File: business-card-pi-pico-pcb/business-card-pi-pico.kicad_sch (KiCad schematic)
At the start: 44 parts, among them U1 Pico

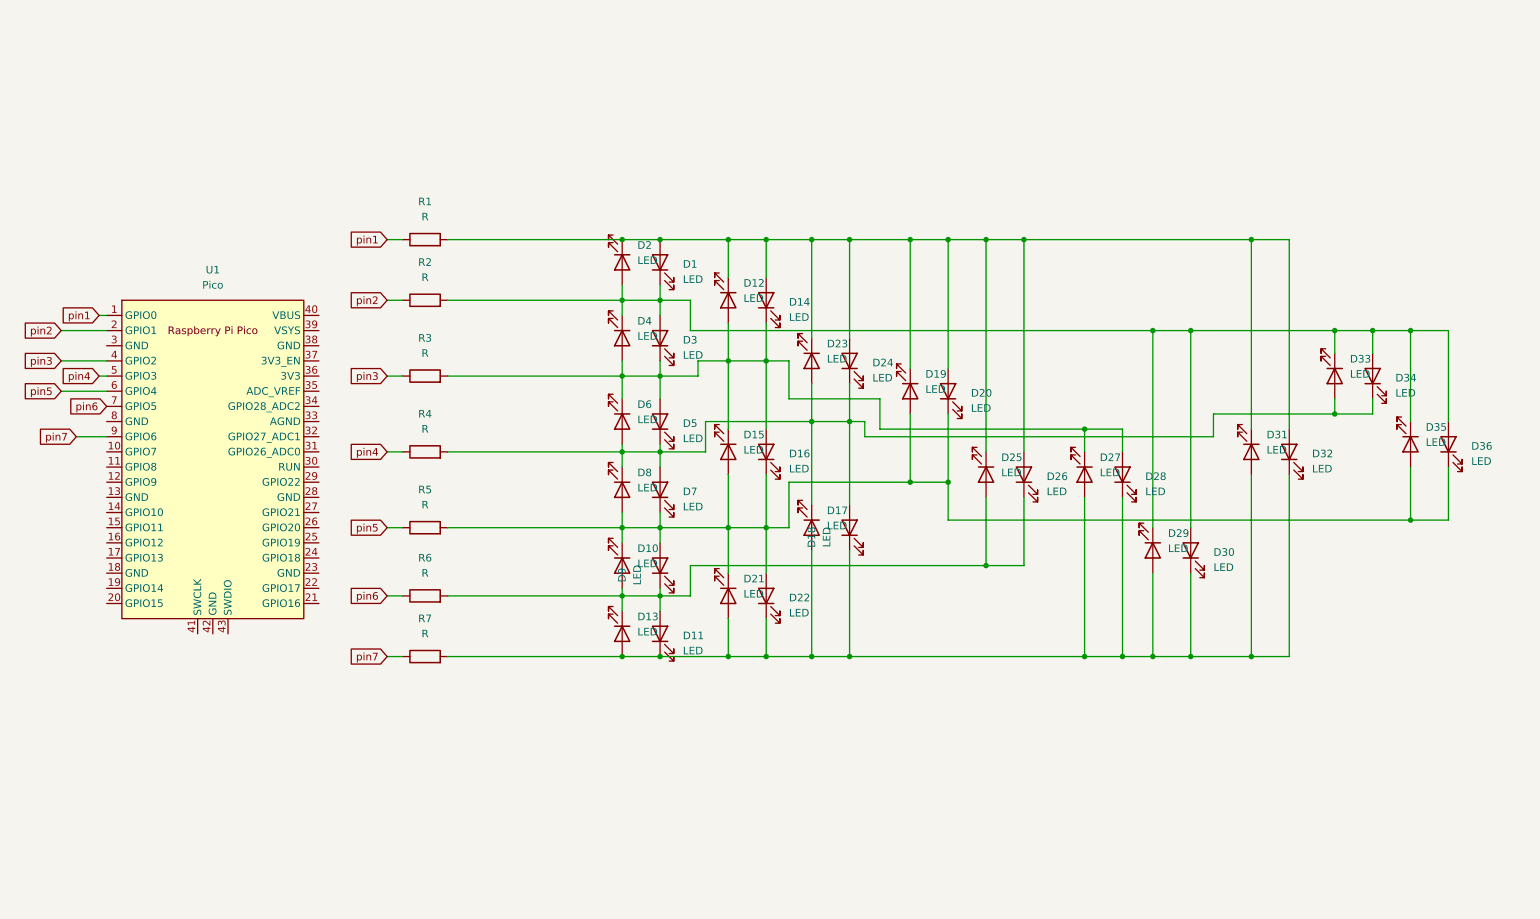
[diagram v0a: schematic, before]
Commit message: added SSD13006 display
added SSD13006 display and push button
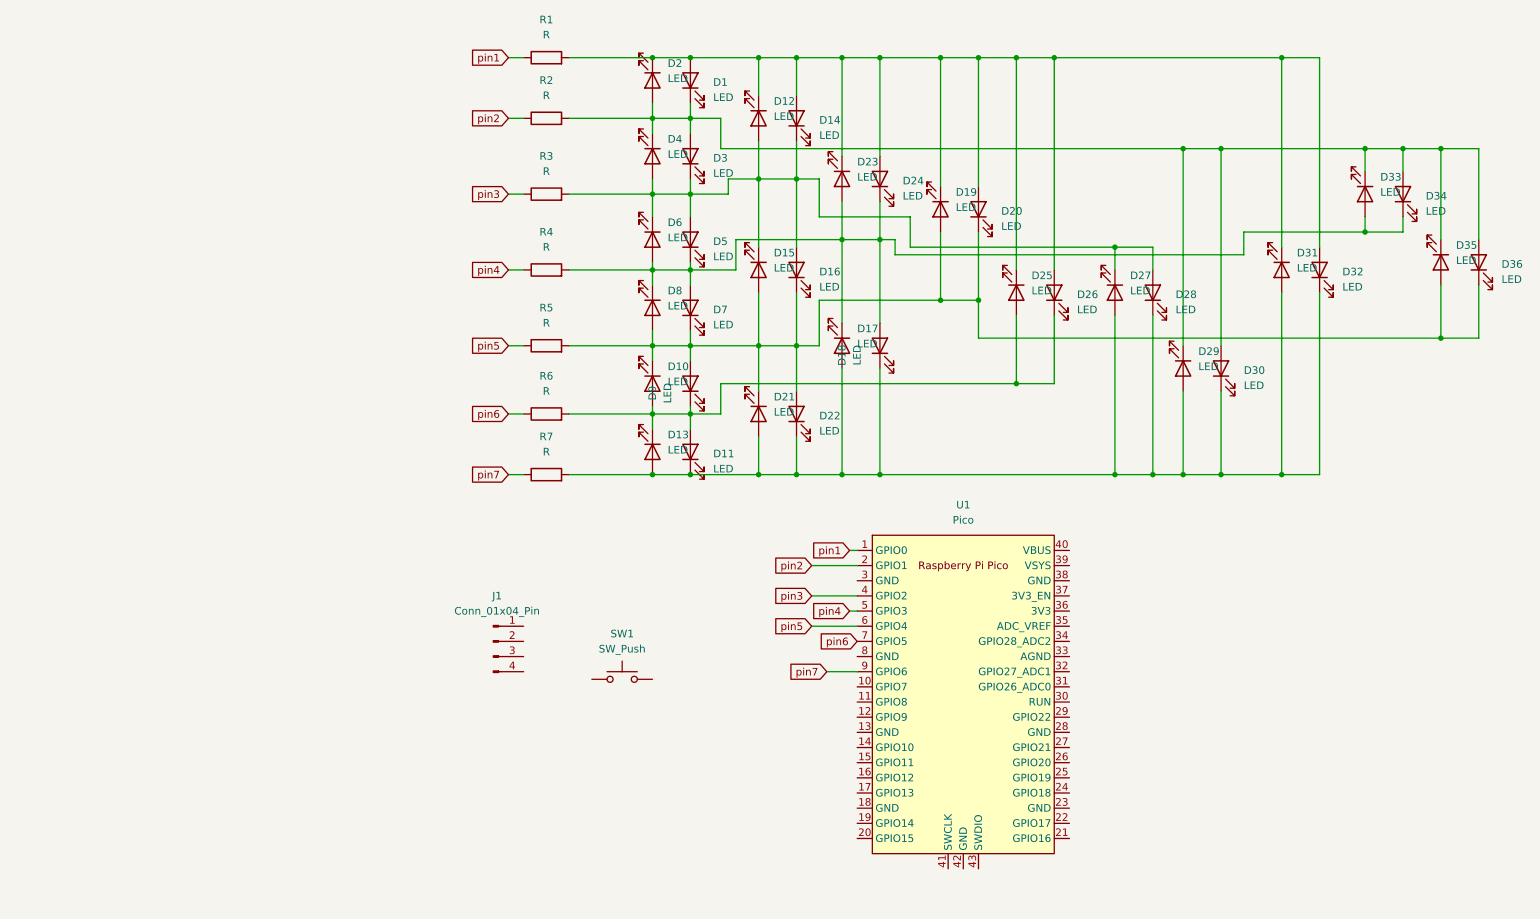
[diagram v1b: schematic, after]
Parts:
- added J1: Conn_01x04_Pin, Display:Adafruit_SSD1306, symbol Connector:Conn_01x04_Pin
- added SW1: SW_Push, Button_Switch_THT:SW_PUSH_6mm_H8mm, symbol Switch:SW_Push
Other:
- moved on the sheet: D1, D10, D11, D12, D13, D14, D15, D16, D17, D18, D19, D2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

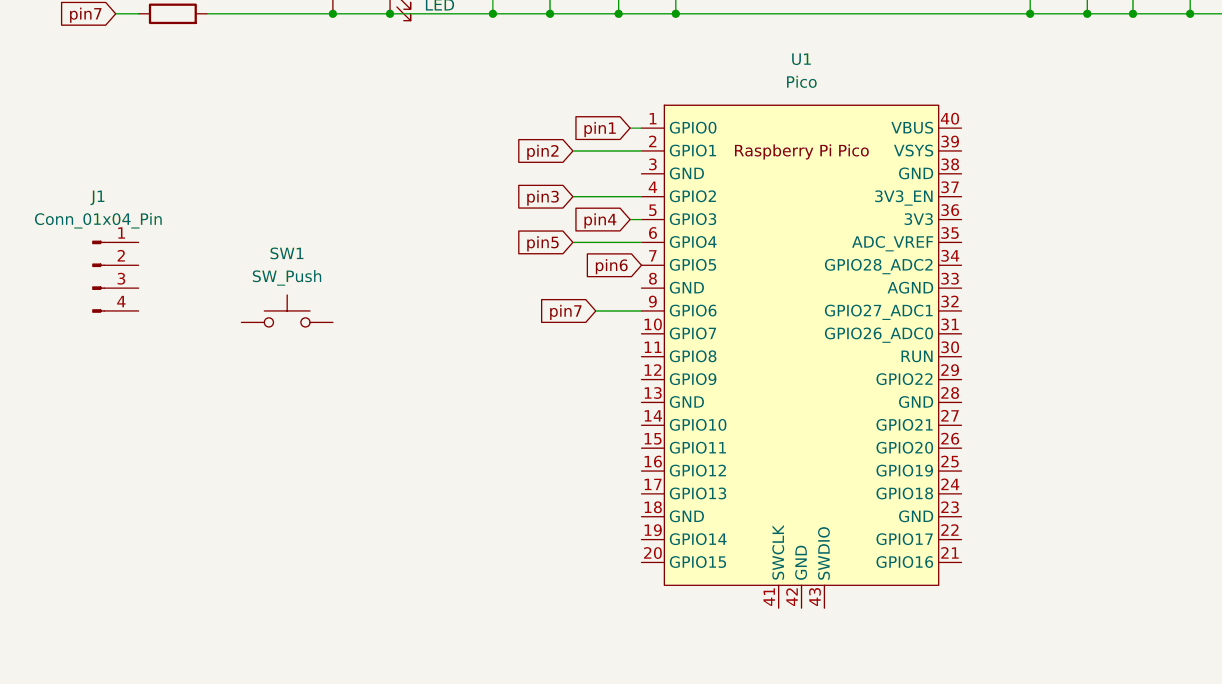
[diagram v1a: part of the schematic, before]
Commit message: Continue working on PCB
Continue working on PCB, added button/touch input pin
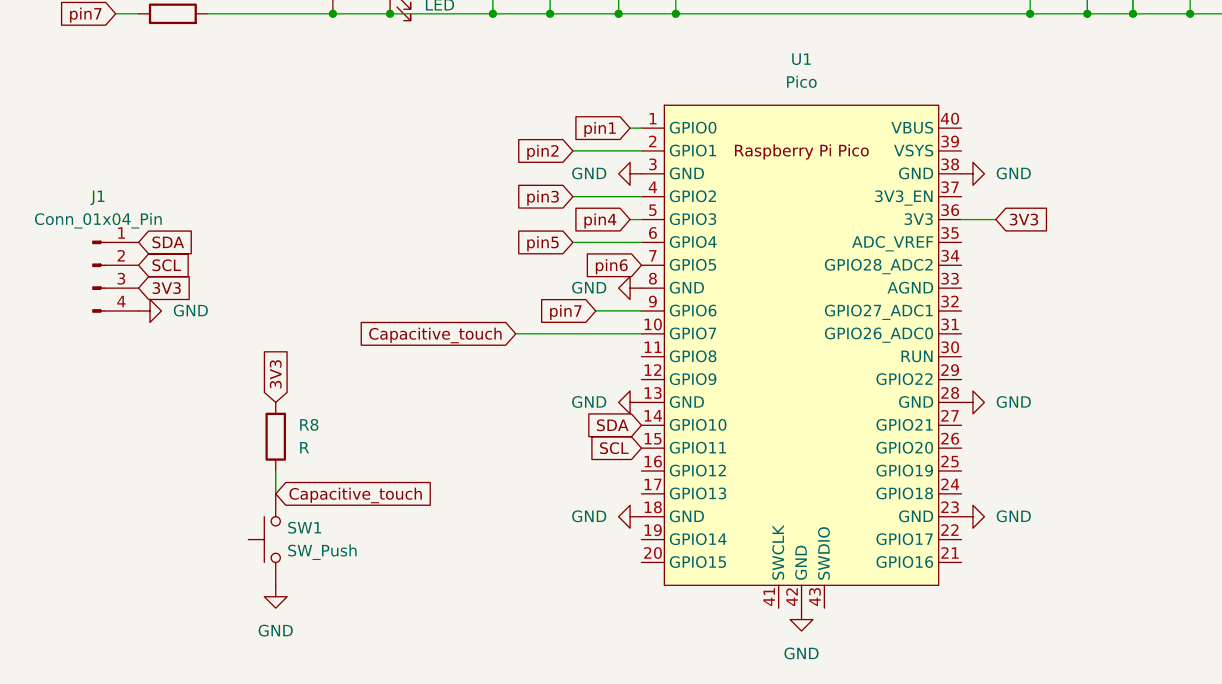
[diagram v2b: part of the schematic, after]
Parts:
- added R8: R, Resistor_SMD:R_0805_2012Metric, symbol Device:R
- J1: footprint Display:Adafruit_SSD1306 -> SSD1306:128x64OLED
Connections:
- net Capacitive_touch: now reaches U1.10 (GPIO7)
- net Capacitive_touch: now also SW1.2, R8.1
- net GND: now reaches U1.13 (GND)
- net GND: now also J1.4 (Pin_4), SW1.1, U1.18 (GND), U1.23 (GND), U1.28 (GND), U1.3 (GND), U1.38 (GND), U1.42 (GND), U1.8 (GND)
- net SDA: now reaches U1.14 (GPIO10)
- net SDA: now also J1.1 (Pin_1)
- net SCL: now reaches U1.15 (GPIO11)
- net SCL: now also J1.2 (Pin_2)
- net 3V3: now reaches U1.36 (3V3)
- net 3V3: now also J1.3 (Pin_3), R8.2
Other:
- moved on the sheet: SW1

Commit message: updated PCB
updated PCB
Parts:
- added R9: R, Resistor_SMD:R_0805_2012Metric, symbol Device:R
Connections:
- net Capacitive_touch: now also R9.2; no longer R8.1, SW1.2
- new net: R8.1, R9.1, SW1.2
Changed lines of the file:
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@@
 	)
 	(junction
+		(at 129.54 142.24)
+		(diameter 0)
+		(color 0 0 0 0)
+	)
+	(junction
 		(at 173.99 91.44)
 		(diameter 0)
@@
 	(wire
 		(pts
+			(xy 129.54 142.24) (xy 129.54 144.78)
+		)
+		(stroke
+			(width 0)
+			(type default)
+		)
+	)
+	(wire
+		(pts
 			(xy 173.99 52.07) (xy 173.99 66.04)
 		)
@@
 	(wire
 		(pts
-			(xy 129.54 142.24) (xy 129.54 144.78)
-		)
-		(stroke
-			(width 0)
-			(type default)
-		)
-	)
-	(wire
-		(pts
 			(xy 160.02 69.85) (xy 160.02 77.47)
 		)
@@
 	(wire
 		(pts
+			(xy 129.54 142.24) (xy 133.35 142.24)
+		)
+		(stroke
+			(width 0)
+			(type default)
+		)
+	)
+	(wire
+		(pts
 			(xy 121.92 31.75) (xy 135.89 31.75)
 		)
@@
 		)
 	)
+	(global_label "Capacitive_touch"
+		(shape input)
+		(at 140.97 142.24 0)
+		(fields_autoplaced yes)
+		(effects
+			(font
+				(size 1.27 1.27)
+			)
+			(justify left)
+		)
+		(property "Intersheetrefs" "${INTERSHEET_REFS}"
+			(at 159.9812 142.24 0)
+			(effects
+				(font
+					(size 1.27 1.27)
+				)
+				(justify left)
+				(hide yes)
+			)
+		)
+	)
 	(global_label "pin5"
 		(shape input)
@@
 		)
 	)
-	(global_label "Capacitive_touch"
-		(shape input)
-		(at 129.54 144.78 0)
-		(fields_autoplaced yes)
-		(effects
-			(font
-				(size 1.27 1.27)
-			)
-			(justify left)
-		)
-		(property "Intersheetrefs" "${INTERSHEET_REFS}"
-			(at 148.5512 144.78 0)
-			(effects
-				(font
-					(size 1.27 1.27)
-				)
-				(justify left)
-				(hide yes)
-			)
-		)
-	)
 	(global_label "pin7"
 		(shape input)
@@
 					(unit 1)
 				)
+			)
+		)
+	)
+	(symbol
+		(lib_id "Device:R")
+		(at 137.16 142.24 90)
+		(unit 1)
+		(exclude_from_sim no)
+		(in_bom yes)
+		(on_board yes)
+		(dnp no)
+		(fields_autoplaced yes)
+		(property "Reference" "R9"
+			(at 137.16 135.89 90)
+			(effects
+				(font
+					(size 1.27 1.27)
+				)
+			)
+		)
+		(property "Value" "R"
+			(at 137.16 138.43 90)
+			(effects
+				(font
+					(size 1.27 1.27)
+				)
+			)
+		)
+		(property "Footprint" "Resistor_SMD:R_0805_2012Metric"
+			(at 137.16 144.018 90)
+			(effects
+				(font
+					(size 1.27 1.27)
+				)
+				(hide yes)
+			)
+		)
+		(property "Datasheet" "~"
+			(at 137.16 142.24 0)
+			(effects
+				(font
+					(size 1.27 1.27)
+				)
+				(hide yes)
+			)
+		)
+		(property "Description" "Resistor"
+			(at 137.16 142.24 0)
+			(effects
+				(font
+					(size 1.27 1.27)
+				)
+				(hide yes)
+			)
+		)
+		(pin "2"
+		)
+		(pin "1"
+		)
+		(instances
+			(project "business-card-pi-pico"
+				(path "/3e5122c1-1f9e-4892-9d66-f0f99c7e104b"
+					(reference "R9")
+					(unit 1)
+				)

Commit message: backups
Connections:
- net 3V3: now also J1.1 (Pin_1); no longer J1.3 (Pin_3)
- net GND: now also J1.2 (Pin_2); no longer J1.4 (Pin_4)
- net SCL: now also J1.3 (Pin_3); no longer J1.2 (Pin_2)
- net SDA: now also J1.4 (Pin_4); no longer J1.1 (Pin_1)
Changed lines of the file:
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@@
 		)
 	)
-	(global_label "3V3"
+	(global_label "pin2"
 		(shape input)
-		(at 114.3 121.92 0)
+		(at 111.76 31.75 180)
 		(fields_autoplaced yes)
 		(effects
@@
 				(size 1.27 1.27)
 			)
-			(justify left)
+			(justify right)
 		)
 		(property "Intersheetrefs" "${INTERSHEET_REFS}"
-			(at 120.7928 121.92 0)
+			(at 104.6625 31.75 0)
 			(effects
 				(font
 					(size 1.27 1.27)
 				)
-				(justify left)
+				(justify right)
 				(hide yes)
 			)
 		)
 	)
-	(global_label "pin2"
+	(global_label "pin5"
 		(shape input)
-		(at 111.76 31.75 180)
+		(at 111.76 69.85 180)
 		(fields_autoplaced yes)
 		(effects
@@
 		)
 		(property "Intersheetrefs" "${INTERSHEET_REFS}"
-			(at 104.6625 31.75 0)
+			(at 104.6625 69.85 0)
 			(effects
 				(font
@@
 		)
 	)
-	(global_label "pin5"
+	(global_label "pin2"
 		(shape input)
-		(at 111.76 69.85 180)
+		(at 162.56 106.68 180)
 		(fields_autoplaced yes)
 		(effects
@@
 		)
 		(property "Intersheetrefs" "${INTERSHEET_REFS}"
-			(at 104.6625 69.85 0)
+			(at 155.4625 106.68 0)
 			(effects
 				(font
@@
 	(global_label "SCL"
 		(shape input)
-		(at 114.3 119.38 0)
+		(at 170.18 139.7 180)
 		(fields_autoplaced yes)
 		(effects
@@
 				(size 1.27 1.27)
 			)
-			(justify left)
+			(justify right)
 		)
 		(property "Intersheetrefs" "${INTERSHEET_REFS}"
-			(at 120.7928 119.38 0)
+			(at 163.6872 139.7 0)
 			(effects
 				(font
 					(size 1.27 1.27)
 				)
-				(justify left)
+				(justify right)
 				(hide yes)
 			)
 		)
 	)
-	(global_label "pin2"
+	(global_label "pin1"
 		(shape input)
-		(at 162.56 106.68 180)
+		(at 168.91 104.14 180)
 		(fields_autoplaced yes)
 		(effects
@@
 		)
 		(property "Intersheetrefs" "${INTERSHEET_REFS}"
-			(at 155.4625 106.68 0)
+			(at 161.8125 104.14 0)
 			(effects
 				(font
@@
 		)
 	)
-	(global_label "SCL"
+	(global_label "Capacitive_touch"
 		(shape input)
-		(at 170.18 139.7 180)
+		(at 156.21 127 180)
 		(fields_autoplaced yes)
 		(effects
@@
 		)
 		(property "Intersheetrefs" "${INTERSHEET_REFS}"
-			(at 163.6872 139.7 0)
+			(at 137.1988 127 0)
 			(effects
 				(font
@@
 		)
 	)
-	(global_label "pin1"
+	(global_label "pin4"
 		(shape input)
-		(at 168.91 104.14 180)
+		(at 111.76 57.15 180)
 		(fields_autoplaced yes)
 		(effects
@@
 		)
 		(property "Intersheetrefs" "${INTERSHEET_REFS}"
-			(at 161.8125 104.14 0)
+			(at 104.6625 57.15 0)
 			(effects
 				(font
@@
 		)
 	)
-	(global_label "Capacitive_touch"
+	(global_label "pin7"
 		(shape input)
-		(at 156.21 127 180)
+		(at 165.1 124.46 180)
 		(fields_autoplaced yes)
 		(effects
@@
 		)
 		(property "Intersheetrefs" "${INTERSHEET_REFS}"
-			(at 137.1988 127 0)
+			(at 158.0025 124.46 0)
 			(effects
 				(font
@@
 		)
 	)
-	(global_label "SDA"
+	(global_label "pin3"
 		(shape input)
-		(at 114.3 116.84 0)
+		(at 111.76 44.45 180)
 		(fields_autoplaced yes)
 		(effects
@@
 				(size 1.27 1.27)
 			)
-			(justify left)
+			(justify right)
 		)
 		(property "Intersheetrefs" "${INTERSHEET_REFS}"
-			(at 120.8533 116.84 0)
+			(at 104.6625 44.45 0)
 			(effects
 				(font
 					(size 1.27 1.27)
 				)
-				(justify left)
+				(justify right)
 				(hide yes)
 			)
 		)
 	)
-	(global_label "pin4"
+	(global_label "pin6"
 		(shape input)
-		(at 111.76 57.15 180)
+		(at 111.76 81.28 180)
 		(fields_autoplaced yes)
 		(effects
@@
 		)
 		(property "Intersheetrefs" "${INTERSHEET_REFS}"
-			(at 104.6625 57.15 0)
+			(at 104.6625 81.28 0)
 			(effects
 				(font
@@
 		)
 	)
-	(global_label "pin7"
+	(global_label "SDA"
 		(shape input)
-		(at 165.1 124.46 180)
+		(at 170.18 137.16 180)
 		(fields_autoplaced yes)
 		(effects
@@
 		)
 		(property "Intersheetrefs" "${INTERSHEET_REFS}"
-			(at 158.0025 124.46 0)
+			(at 163.6267 137.16 0)
 			(effects
 				(font
@@
 		)
 	)
-	(global_label "pin3"
+	(global_label "SDA"
 		(shape input)
-		(at 111.76 44.45 180)
+		(at 114.3 124.46 0)
 		(fields_autoplaced yes)
 		(effects
@@
 				(size 1.27 1.27)
 			)
-			(justify right)
+			(justify left)
 		)
 		(property "Intersheetrefs" "${INTERSHEET_REFS}"
-			(at 104.6625 44.45 0)
+			(at 120.8533 124.46 0)
 			(effects
 				(font
 					(size 1.27 1.27)
 				)
-				(justify right)
+				(justify left)
 				(hide yes)
 			)
@@
 	(global_label "pin6"
 		(shape input)
-		(at 111.76 81.28 180)
+		(at 170.18 119.38 180)
 		(fields_autoplaced yes)
 		(effects
@@
 		)
 		(property "Intersheetrefs" "${INTERSHEET_REFS}"
-			(at 104.6625 81.28 0)
+			(at 163.0825 119.38 0)
 			(effects
 				(font
@@
 		)
 	)
-	(global_label "SDA"
+	(global_label "3V3"
 		(shape input)
-		(at 170.18 137.16 180)
+		(at 129.54 134.62 90)
 		(fields_autoplaced yes)
 		(effects
@@
 				(size 1.27 1.27)
 			)
-			(justify right)
+			(justify left)
 		)
 		(property "Intersheetrefs" "${INTERSHEET_REFS}"
-			(at 163.6267 137.16 0)
+			(at 129.54 128.1272 90)
 			(effects
 				(font
 					(size 1.27 1.27)
 				)
-				(justify right)
+				(justify left)
 				(hide yes)
 			)
 		)
 	)
-	(global_label "pin6"
+	(global_label "pin1"
 		(shape input)
-		(at 170.18 119.38 180)
+		(at 111.76 21.59 180)
 		(fields_autoplaced yes)
 		(effects
@@
 		)
 		(property "Intersheetrefs" "${INTERSHEET_REFS}"
-			(at 163.0825 119.38 0)
+			(at 104.6625 21.59 0)
 			(effects
 				(font
@@
 		)
 	)
-	(global_label "3V3"
+	(global_label "SCL"
 		(shape input)
-		(at 129.54 134.62 90)
+		(at 114.3 121.92 0)
 		(fields_autoplaced yes)
 		(effects
@@
 		)
 		(property "Intersheetrefs" "${INTERSHEET_REFS}"
-			(at 129.54 128.1272 90)
+			(at 120.7928 121.92 0)
 			(effects
 				(font
@@
 		)
 	)
-	(global_label "pin1"
+	(global_label "3V3"
 		(shape input)
-		(at 111.76 21.59 180)
+		(at 114.3 116.84 0)
 		(fields_autoplaced yes)
 		(effects
@@
 				(size 1.27 1.27)
 			)
-			(justify right)
+			(justify left)
 		)
 		(property "Intersheetrefs" "${INTERSHEET_REFS}"
-			(at 104.6625 21.59 0)
+			(at 120.7928 116.84 0)
 			(effects
 				(font
 					(size 1.27 1.27)
 				)
-				(justify right)
+				(justify left)
 				(hide yes)
 			)
@@
 	(symbol
 		(lib_id "power:GND")
-		(at 114.3 124.46 90)
-		(unit 1)
-		(exclude_from_sim no)
-		(in_bom yes)
-		(on_board yes)
-		(dnp no)
-		(fields_autoplaced yes)
-		(property "Reference" "#PWR010"
-			(at 120.65 124.46 0)
-			(effects
-				(font
-					(size 1.27 1.27)
-				)
-				(hide yes)
-			)
-		)
-		(property "Value" "GND"
-			(at 118.11 124.4599 90)
-			(effects
-				(font
-					(size 1.27 1.27)
-				)
-				(justify right)
-			)
-		)
-		(property "Footprint" ""
-			(at 114.3 124.46 0)
-			(effects
-				(font
-					(size 1.27 1.27)
-				)
-				(hide yes)
-			)
-		)
-		(property "Datasheet" ""
-			(at 114.3 124.46 0)
-			(effects
-				(font
-					(size 1.27 1.27)
-				)
-				(hide yes)
-			)
-		)
-		(property "Description" "Power symbol creates a global label with name \"GND\" , ground"
-			(at 114.3 124.46 0)
-			(effects
-				(font
-					(size 1.27 1.27)
-				)
-				(hide yes)
-			)
-		)
-		(pin "1"
-		)
-		(instances
-			(project "business-card-pi-pico"
-				(path "/3e5122c1-1f9e-4892-9d66-f0f99c7e104b"
-					(reference "#PWR010")
-					(unit 1)
-				)
-			)
-		)
-	)
-	(symbol
-		(lib_id "power:GND")
 		(at 170.18 147.32 270)
 		(unit 1)
@@
 					(unit 1)
 				)
+			)
+		)
+	)
+	(symbol
+		(lib_id "power:GND")
+		(at 114.3 119.38 90)
+		(unit 1)
+		(exclude_from_sim no)
+		(in_bom yes)
+		(on_board yes)
+		(dnp no)
+		(fields_autoplaced yes)
+		(property "Reference" "#PWR010"
+			(at 120.65 119.38 0)
+			(effects
+				(font
+					(size 1.27 1.27)
+				)
+				(hide yes)
+			)
+		)
+		(property "Value" "GND"
+			(at 118.11 119.3799 90)
+			(effects
+				(font
+					(size 1.27 1.27)
+				)
+				(justify right)
+			)
+		)
+		(property "Footprint" ""
+			(at 114.3 119.38 0)
+			(effects
+				(font
+					(size 1.27 1.27)
+				)
+				(hide yes)
+			)
+		)
+		(property "Datasheet" ""
+			(at 114.3 119.38 0)
+			(effects
+				(font
+					(size 1.27 1.27)
+				)
+				(hide yes)
+			)
+		)
+		(property "Description" "Power symbol creates a global label with name \"GND\" , ground"
+			(at 114.3 119.38 0)
+			(effects
+				(font
+					(size 1.27 1.27)
+				)
+				(hide yes)
+			)
+		)
+		(pin "1"
+		)
+		(instances
+			(project "business-card-pi-pico"
+				(path "/3e5122c1-1f9e-4892-9d66-f0f99c7e104b"
+					(reference "#PWR010")
+					(unit 1)
+				)
